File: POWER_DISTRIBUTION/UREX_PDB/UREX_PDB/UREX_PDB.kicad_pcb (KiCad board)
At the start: 4 copper layers, 89.8 x 59.7 mm, 128 parts, among them IC1 TCAN1044VDDFR, IC10 TPS22997RYZR, IC2 TPS1HB08BQPWPRQ1, IC3 TPS1HB08BQPWPRQ1, IC4 INA232AIDDFR, IC5 TCA6408ARGTR, IC8 TPS22997RYZR, IC9 TPS22997RYZR, J10 S2B-PH-SM4-TB_LF__SN_, J11 Conn_01x02, J12 S3B-PH-SM4-TB_LF__SN_, J33 Conn_01x02, J34 Conn_01x02, J36 Conn_01x02, J37 Conn_01x02, J4 S2B-PH-SM4-TB_LF__SN_, J5 S3B-PH-SM4-TB_LF__SN_, J6 S4B-PH-SM4-TB_LF__SN_, J7 S2B-PH-SM4-TB_LF__SN_, J8 S3B-PH-SM4-TB_LF__SN_, J9 S6B-PH-SM4-TB_LF__SN_, Q1 RSS070N05HZGTB, Q2 RSS070N05HZGTB, U1 ESP32-WROOM-32UE-R2, U4 PLM1117120QDCYRQ1, U5 XTPS552892RYQR, U7 USBLC6-2SC6

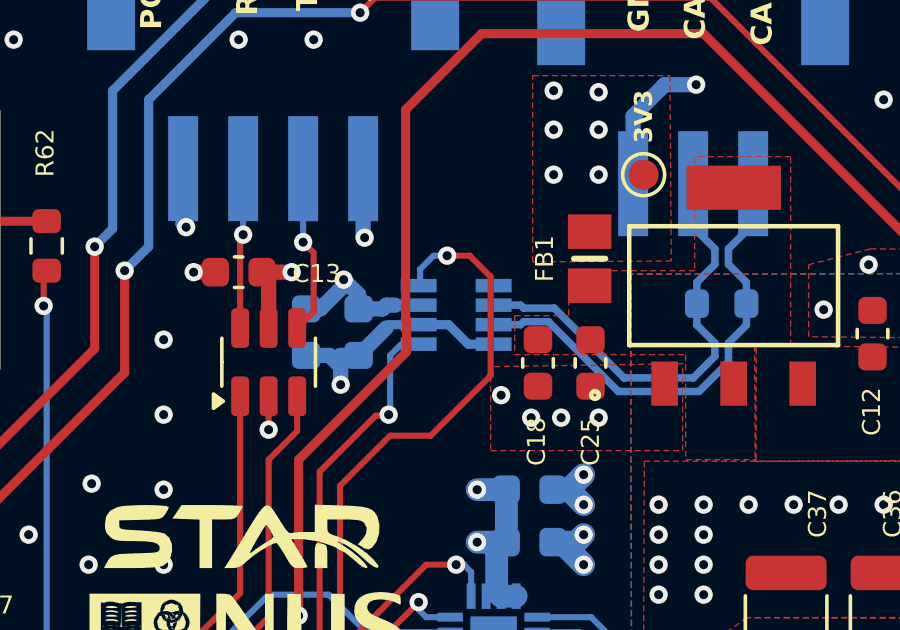
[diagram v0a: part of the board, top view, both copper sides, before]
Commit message: changed CAN IC
TCAN1044 to TCAN332D, pin to pin compatible
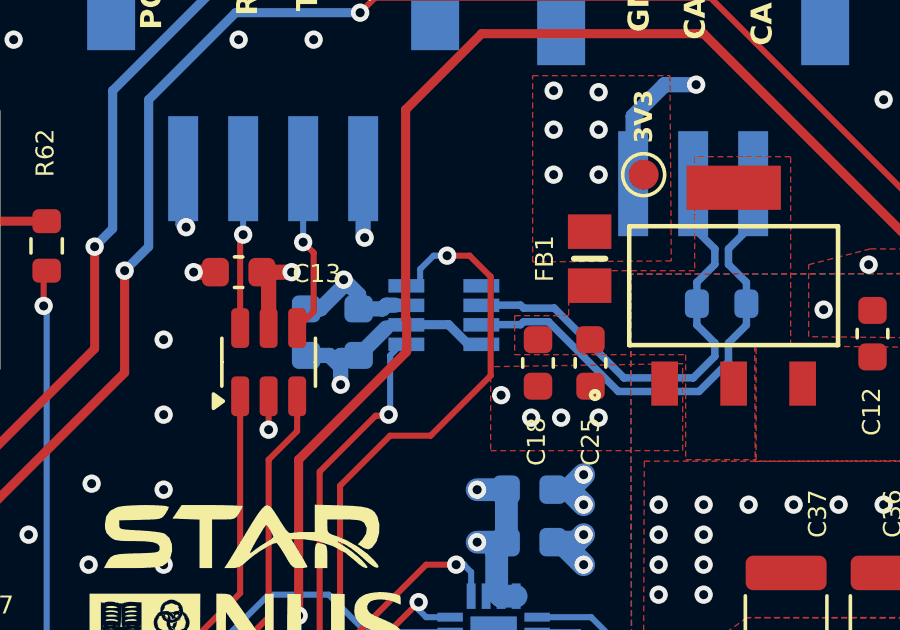
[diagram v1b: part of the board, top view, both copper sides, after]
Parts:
- IC1: value TCAN1044VDDFR -> TCAN332DCNR; footprint SamacSys_Parts:SOT65P280X110-8N -> SamacSys_Parts:SOT65P280X145-8N
- moved IC1 0.41 mm to (101.8, 76.7)
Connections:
- IC1 pad 6: CAN- -> CAN+
- IC1 pad 7: CAN+ -> CAN-
